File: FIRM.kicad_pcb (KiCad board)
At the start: 6 copper layers, 21.3 x 27 mm, 81 parts, among them J1 DM3CS-SF, J2 Conn_01x02_Pin, Q1 IRLML6402, U1 W25Q128JVP, U2 STM32F405RGTx, U3 ADXL371, U5 INA219AxDCN, U6 MIC5219-3.3YM5, U9 A-USBC-20F0-EA-GSR05, X1 32.768khz, Y1 12 MHz

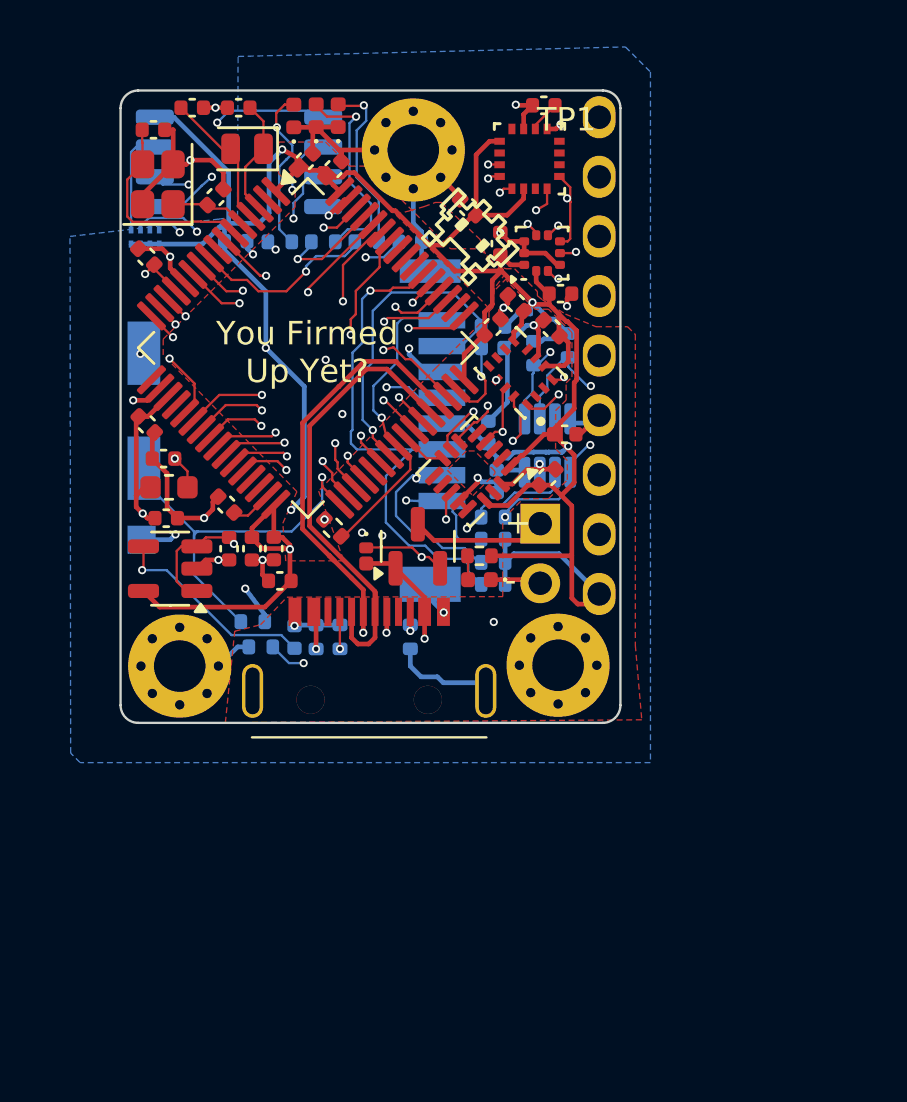
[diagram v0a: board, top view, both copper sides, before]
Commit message: Fixed Most Errors
Mostly just spacing things out. One error remaining.
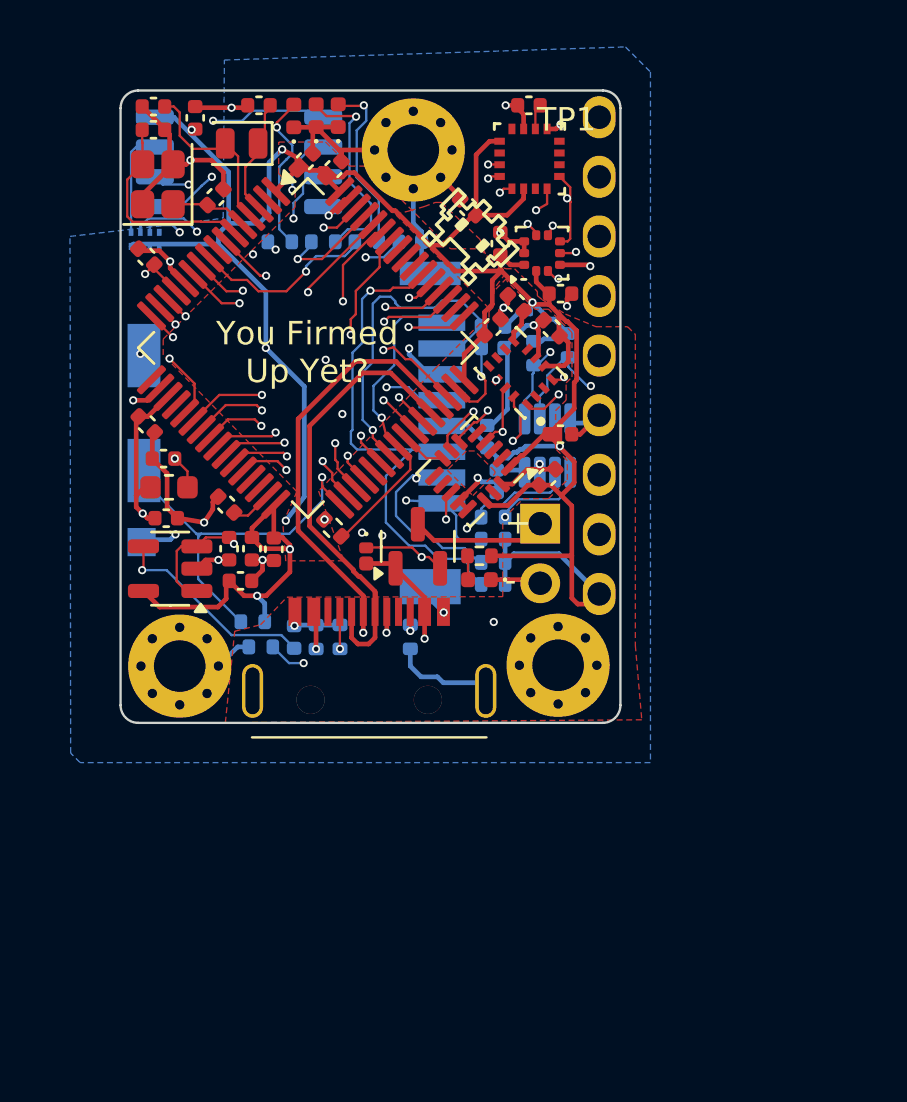
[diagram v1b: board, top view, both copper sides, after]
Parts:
- C12: moved to F.Cu
- moved C12 5.53 mm to (156.5, 75.7), turned to -90 degrees
- moved C28 1.68 mm to (158.4, 95.5), turned to 0 degrees
- moved C7 1.65 mm to (154.7, 75.3), turned to 180 degrees
- moved C4 0.87 mm to (159.2, 75.2)
- moved C30 0.63 mm to (170.7, 75.2)
- moved X1 0.32 mm to (158.5, 76.8)
- moved C11 0.18 mm to (169.0, 89.3)
- moved C19 0.18 mm to (172.1, 89.2)
- moved J1 0.10 mm to (160.7, 89.0)
- moved RN2 0.10 mm to (154.4, 80.9)
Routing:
- net +3.3V: track 148.2 -> 142.9 mm, vias 10 -> 11
- net /VSENS_IN: track 14.7 -> 12.8 mm, vias 3 -> 2
- net /LSE_OUT: track 6.08 -> 7.56 mm
- net GND: track 78.3 -> 79.7 mm, vias 22 -> 23
- net /MOSI2: track 34.1 -> 32.9 mm
- net /SCK2: track 27.7 -> 28.7 mm
- net /MISO2: track 30.7 -> 30.0 mm
- net VBUS: track 12.2 -> 11.7 mm
- net Net-(U2-VDDA): track 12.4 -> 11.9 mm

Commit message: Modified Schottky Barrier Diode, Connected +3.3v
0 errors now, +3.3v is connected correctly.
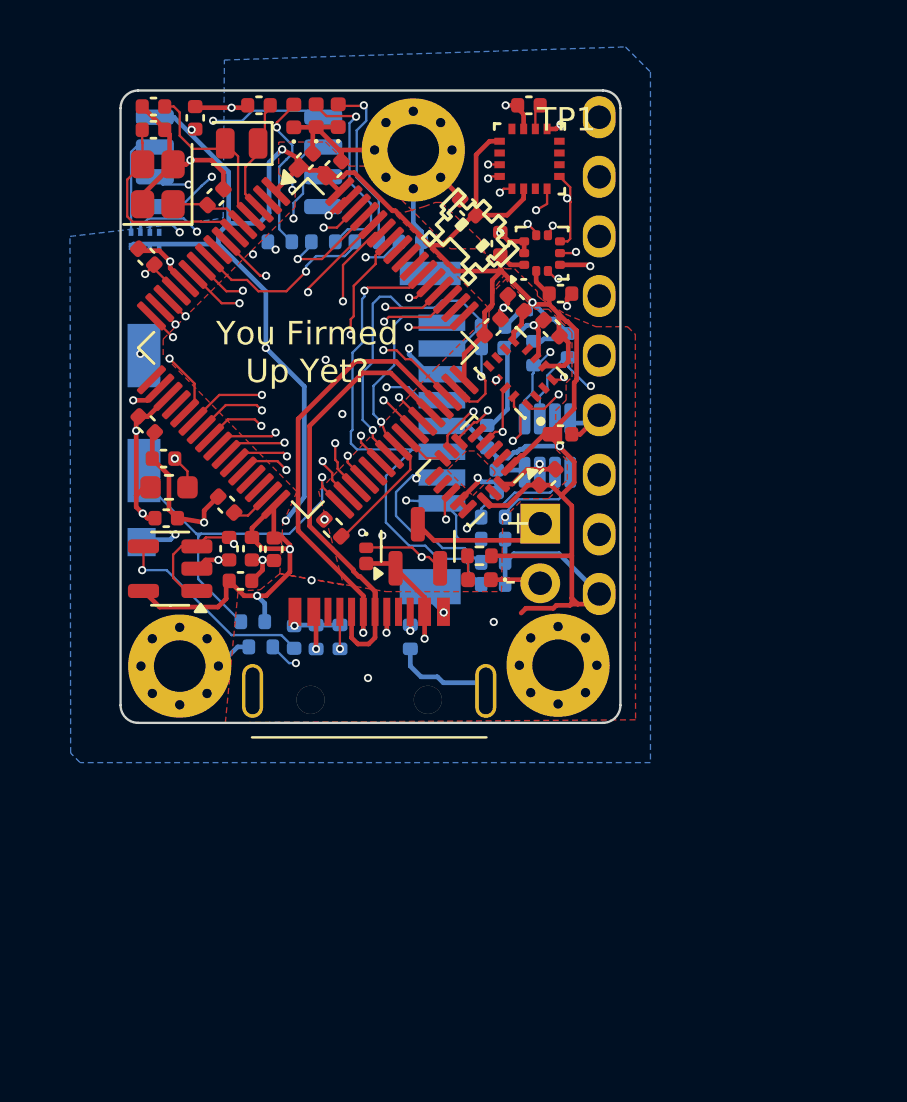
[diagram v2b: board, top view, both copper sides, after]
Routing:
- net +3.3V: track 142.9 -> 147.4 mm, vias 11 -> 13
- net /SDIO_D3: track 18.6 -> 19.6 mm
- net /SCK2: track 28.7 -> 29.2 mm
- net /BOOT0: vias 2 -> 3

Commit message: Teardrops, Better Power Connections
💧
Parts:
- moved C20 0.14 mm to (171.6, 90.9)
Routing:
- net +3.3V: track 147.4 -> 147.5 mm, vias 13 -> 15

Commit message: 8 Layer Conversion
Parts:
- moved C18 0.12 mm to (155.3, 92.7)
- moved U6 0.12 mm to (155.4, 94.8)
- moved C17 0.10 mm to (155.1, 90.2)
- moved C8 0.10 mm to (154.4, 88.8)
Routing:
- net +3.3V: track 147.5 -> 155.4 mm, vias 15 -> 17
- net /MISO2: track 29.7 -> 33.5 mm
- net /MOSI2: track 32.8 -> 31.9 mm
- net Net-(U6-BP): track 8.90 -> 8.36 mm
- added copper zone on In4.Cu, net +3.3V
- added copper zone on In5.Cu, net GND
- added copper zone on In6.Cu, net GND
- removed copper zone on In4.Cu, net GND
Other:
- copper layers 6 -> 8

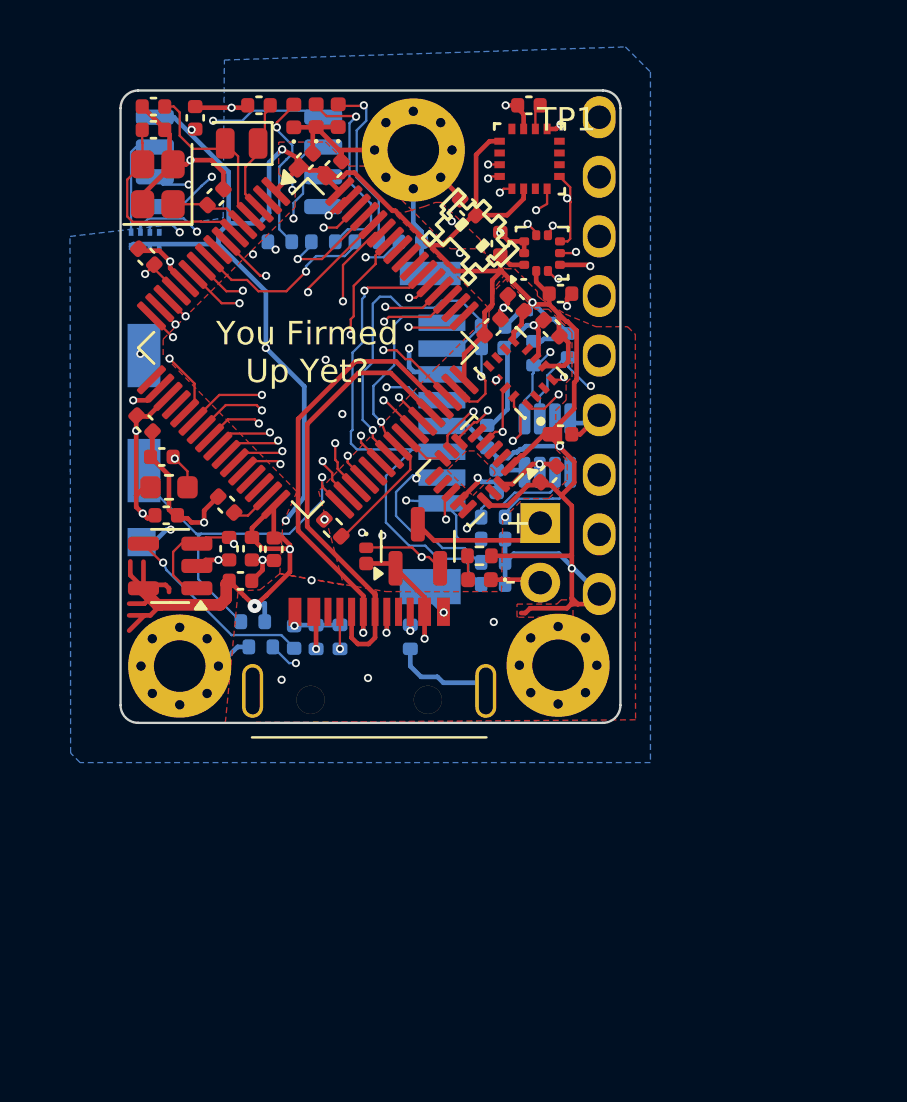
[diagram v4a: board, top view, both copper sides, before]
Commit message: Increased Via Size
Via hole is now 0.3mm and Via diameter is 0.5mm. Everything fits, no board resizing needed.
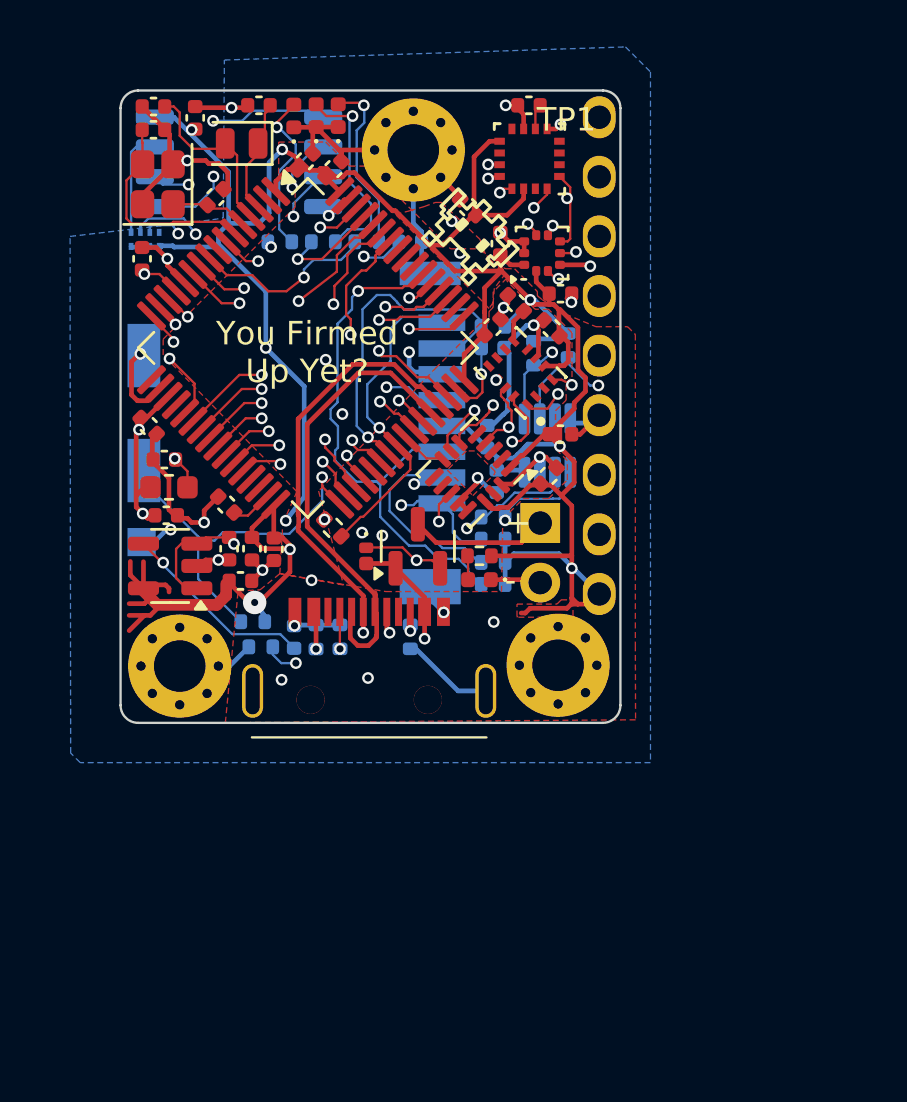
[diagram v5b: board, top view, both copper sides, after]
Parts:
- moved C8 0.21 mm to (154.5, 88.9)
- moved C16 0.20 mm to (154.2, 81.8), turned to 90 degrees
- moved C17 0.16 mm to (155.2, 90.3)
- moved C20 0.07 mm to (171.6, 91.0)
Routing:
- net GND: track 80.2 -> 82.1 mm, vias 23 -> 21
- net /MOSI2: track 31.9 -> 33.3 mm
- net /IMU_INT: track 22.0 -> 23.0 mm
- net /HIG_INT: track 11.8 -> 12.7 mm
- net /SWDIO: track 13.4 -> 14.2 mm
- net /SDIO_D3: track 19.6 -> 20.4 mm
- net +3.3V: track 155.4 -> 156.2 mm
- net /BOOT0: track 22.5 -> 23.2 mm
- net /DBUG_2: track 11.2 -> 10.5 mm
- net /SDIO_D2: track 16.1 -> 16.9 mm
- net /PA0: track 23.1 -> 23.8 mm
- net /MAG_INT: track 23.5 -> 22.8 mm
- net /MISO1: track 16.7 -> 16.0 mm
- net /MISO2: track 33.5 -> 34.1 mm
- net Net-(U2-VDDA): track 11.9 -> 11.4 mm
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
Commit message: Small Improvements
Slightly better via techniques, better heat-sink-ish copper pour for the voltage regulator
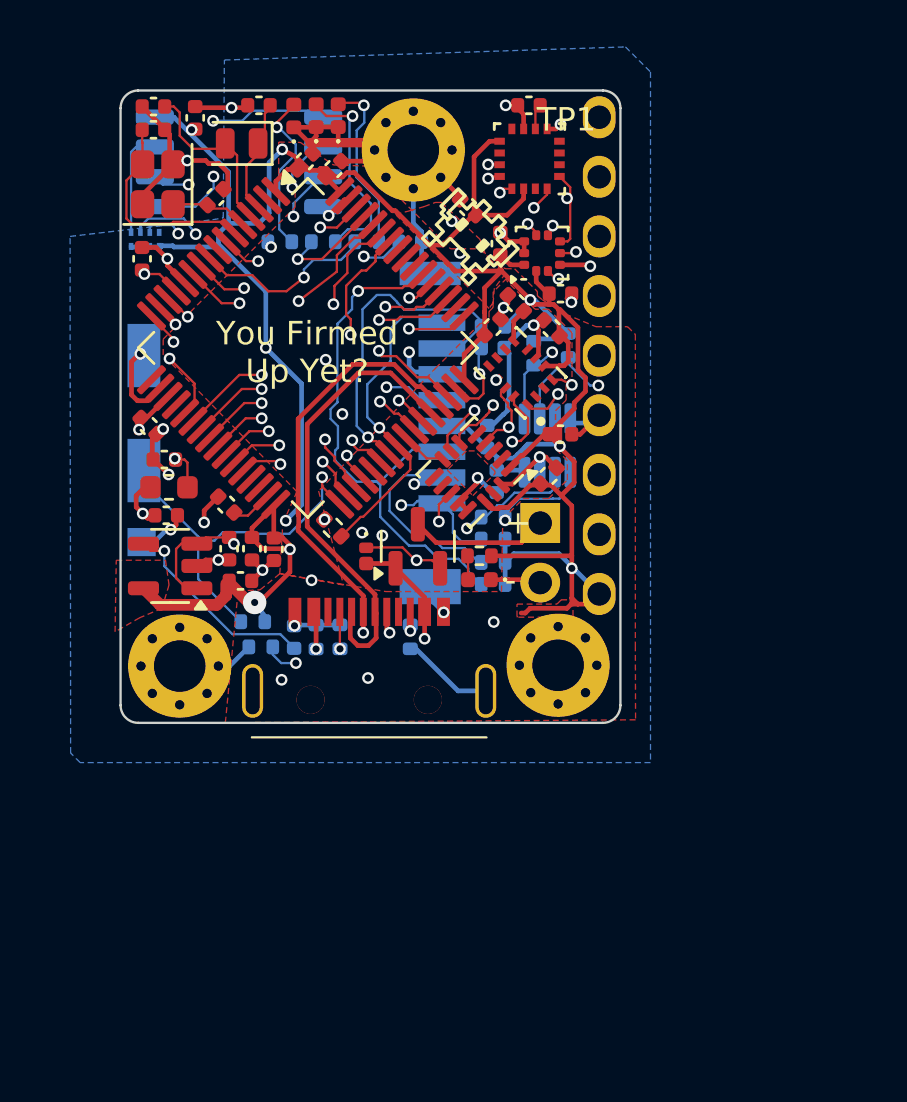
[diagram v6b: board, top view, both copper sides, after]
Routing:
- net +3.3V: track 156.2 -> 146.1 mm
- net /USB_D-: track 20.6 -> 19.7 mm
- net GND: track 82.1 -> 82.9 mm, vias 21 -> 23

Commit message: placements
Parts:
- added TP24: NRST Pad, connectors:smd_test_pads_1mm, F.Cu at (169.5, 75.5)
- C1, C14, R1, R11, R12, R13, R14, R15, R16, R2, R20, R21, R3, R4, R5, R7: moved to F.Cu
- C12, C28, C30, D4, Q1, U6: moved to B.Cu
- U1: value W25Q128JVP -> W25Q128JVS
- moved H1 26.6 mm to (154.0, 101.0)
- moved R16 25.1 mm to (183.1, 84.9), turned to 0 degrees
- moved R7 24.6 mm to (180.2, 84.9)
- moved R15 24.4 mm to (180.2, 94.8), turned to 0 degrees
- moved H2 24.2 mm to (166.0, 77.1)
- moved D1 23.5 mm to (152.4, 96.8)
- moved C7 23.0 mm to (172.1, 90.3), turned to 90 degrees
- moved D2 22.8 mm to (153.3, 96.8)
- moved D3 22.1 mm to (154.3, 96.8)
- moved R14 21.7 mm to (180.2, 92.8), turned to 0 degrees
- moved R20 21.6 mm to (183.1, 90.8), turned to 0 degrees
- moved C4 21.1 mm to (171.7, 92.2), turned to 90 degrees
- moved R3 20.3 mm to (177.3, 88.8), turned to 0 degrees
- moved C20 20.2 mm to (152.7, 84.0), turned to 90 degrees
- moved C10 19.9 mm to (172.2, 85.9), turned to 90 degrees
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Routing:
- net +3.3V: track 146.1 -> 0.00 mm, vias 17 -> 0
- net GND: track 82.9 -> 0.00 mm, vias 23 -> 0
- net /MISO2: track 34.1 -> 0.00 mm, vias 4 -> 0
- net /MOSI2: track 33.3 -> 0.00 mm, vias 5 -> 0
- net /SCK2: track 29.7 -> 0.00 mm, vias 4 -> 0
- net /I2C1_SDA: track 26.2 -> 0.00 mm, vias 3 -> 0
- net /FLASH_CS: track 25.9 -> 0.00 mm, vias 3 -> 0
- net /SDIO_CMD: track 24.0 -> 0.00 mm, vias 1 -> 0
- net /PA0: track 23.8 -> 0.00 mm, vias 1 -> 0
- net /BOOT0: track 23.2 -> 0.00 mm, vias 3 -> 0
- net /IMU_INT: track 23.0 -> 0.00 mm, vias 2 -> 0
- net /MAG_INT: track 22.8 -> 0.00 mm, vias 2 -> 0
- net /PA1: track 22.7 -> 0.00 mm, vias 1 -> 0
- net /PA2: track 22.3 -> 0.00 mm, vias 1 -> 0
- net /VSENS_OUT: track 22.2 -> 0.00 mm, vias 2 -> 0
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- removed copper zone on B.Cu, net +3.3V
- removed copper zone on F.Cu, net +3.3V
- removed copper zone on In2.Cu, net +3.3V
- removed copper zone on In4.Cu, net +3.3V
- removed copper zone on F.Cu, net GND
- removed copper zone on In1.Cu, net GND
- removed copper zone on In3.Cu, net GND
- removed copper zone on In5.Cu, net GND
- removed copper zone on In6.Cu, net GND
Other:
- board size 21.3 x 27 mm -> 23.3 x 29.5 mm

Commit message: tweak
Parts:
- moved D4 0.43 mm to (168.8, 97.9)
- moved U9 0.09 mm to (162.2, 102.5)
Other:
- board size 23.3 x 29.5 mm -> 23.3 x 29.6 mm
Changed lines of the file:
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@@
 	(footprint "connectors:A-USBC-20F0-EA-GSR05"
 		(layer "F.Cu")
-		(at 162.16 102.63)
+		(at 162.2 102.55)
 		(property "Reference" "U9"
 			(at 0 12 0)
@@
 	(footprint "connectors:D_schottky_NSR05F30NXT5G"
 		(layer "B.Cu")
-		(at 168.35 97.85 90)
+		(at 168.78 97.86 90)
 		(descr "Diode SMD 0402 (1005 Metric), square (rectangular) end terminal, IPC-7351 nominal, (Body size source: http://www.tortai-tech.com/upload/download/2011102023233369053.pdf), generated with kicad-footprint-generator")
 		(tags "diode")
@@
 	(gr_rect
 		(start 151.45 74.09)
-		(end 174.71 103.59)
+		(end 174.71 103.66)
 		(stroke
 			(width 0.1)
